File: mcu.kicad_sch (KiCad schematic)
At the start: 56 parts, among them IC5 STM32H723ZGT6, J1 Conn_ST_STDC14, J5 Conn_01x08, SW1 RESET, Y1 16MHz

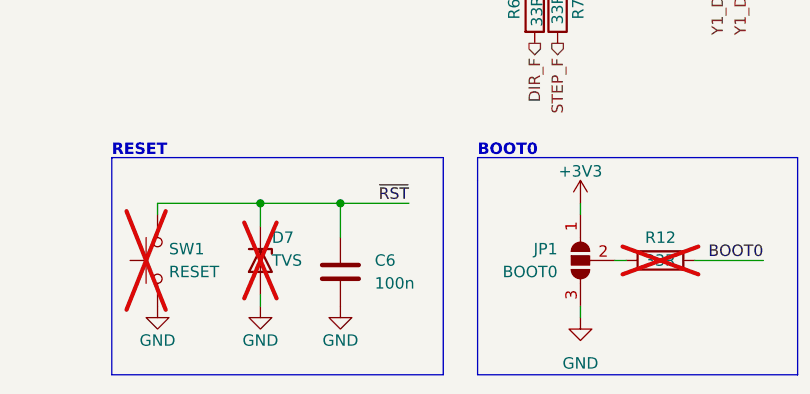
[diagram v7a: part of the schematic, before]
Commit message: fix: DNP for current sensors
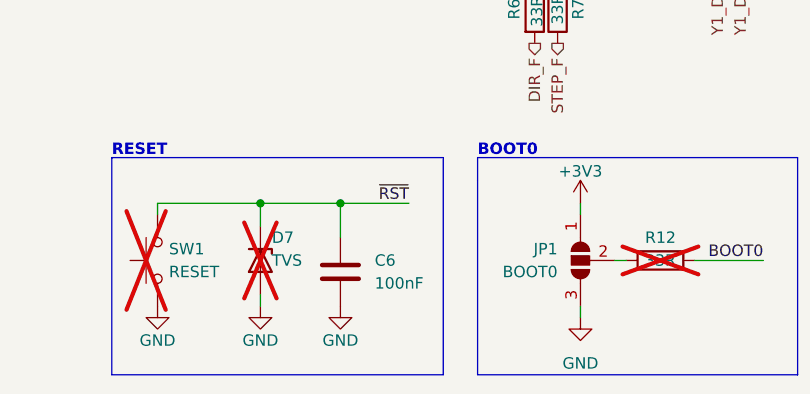
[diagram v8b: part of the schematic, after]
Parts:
- C6: value 100n -> 100nF
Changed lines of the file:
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@@
 			)
 		)
-		(property "Value" "100n"
+		(property "Value" "100nF"
 			(at 200.66 271.78 0)
 			(effects
